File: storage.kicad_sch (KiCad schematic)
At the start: 0 parts

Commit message: Commit
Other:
- note added: "Simpler Flight v2"
- title: (none) -> Storage

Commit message: addecd stuff
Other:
- note added: "Flash Memory"
- note added: "SD Card"
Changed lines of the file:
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@@
 		(title "Storage")
 	)
+	(text "Flash Memory"
+		(exclude_from_sim no)
+		(at 38.608 23.114 0)
+		(effects
+			(font
+				(size 2.54 2.54)
+				(thickness 0.508)
+				(bold yes)
+			)
+		)
+	)
+	(text "SD Card"
+		(exclude_from_sim no)
+		(at 84.074 23.114 0)
+		(effects
+			(font
+				(size 2.54 2.54)
+				(thickness 0.508)
+				(bold yes)
+			)
+		)
+	)
 	(text "Simpler Flight v2\n"
 		(exclude_from_sim no)
@@
 		)
 	)
+	(polyline
+		(pts
+			(xy 76.2 25.4) (xy 119.38 25.4)
+		)
+		(stroke
+			(width 0)
+			(type default)
+		)
+	)
+	(polyline
+		(pts
+			(xy 25.4 25.4) (xy 68.58 25.4)
+		)
+		(stroke
+			(width 0)
+			(type default)
+		)
+	)
+	(polyline
+		(pts
+			(xy 25.4 58.42) (xy 25.4 25.4)
+		)
+		(stroke
+			(width 0)
+			(type default)
+		)
+	)
+	(polyline
+		(pts
+			(xy 119.38 25.4) (xy 119.38 58.42)
+		)
+		(stroke
+			(width 0)
+			(type default)
+		)
+	)
+	(polyline
+		(pts
+			(xy 68.58 58.42) (xy 25.4 58.42)
+		)
+		(stroke
+			(width 0)
+			(type default)
+		)
+	)
+	(polyline
+		(pts
+			(xy 76.2 58.42) (xy 76.2 25.4)
+		)
+		(stroke
+			(width 0)
+			(type default)
+		)
+	)
+	(polyline
+		(pts
+			(xy 68.58 25.4) (xy 68.58 58.42)
+		)
+		(stroke
+			(width 0)
+			(type default)
+		)
+	)
+	(polyline
+		(pts
+			(xy 119.38 58.42) (xy 76.2 58.42)
+		)
+		(stroke
+			(width 0)
+			(type default)
+		)
+	)
 	(image
 		(at 254.508 174.244)
@@
 			"AAAAAAAAAAAAAAAAAAAAAAAAAAAAAAAAAAAAAAAAAAAAAAAAAAAAAAAAAAAAAAAAAAAAAAAAAAAA"
 			"AAAAAAAAAAAAAAAAAAAAAAAAAAAAAAAAAAAAAAAAAAAAAAAAAAAAAAAAAAAAAAAAAAAAAAAAAAAA"
+			"AAAAAAAAAAAAAAAAAAAAAAAAAAAAAAAAAAAAAAAAAAAAAAAAAAAAAAAAAAAAAAAAAAAAAAAAAAAA"
+			"AAAAAAAAAAAAAAAAAAAAAAAAAAAAAAAAAAAAAAAAAAAAAAAAAAAAAAAAAAAAAAAAAAAAAAAAAAAA"
+			"AAAAAAAAAAAAAAAAAAAAAAAAAAAAAAAAAAAAAAAAAAAAAAAAAAAAAAAAAAAAAAAAAAAAAAAAAAAA"
+			"AAAAAAAAAAAAAAAAAAAAAAAAAAAAAAAAAAAAAAAAAAAAAAAAAAAAAAAAAAAAAAAAAAAAAAAAAAAA"
+			"AAAAAAAAAAAAAAAAAAAAAAAAAAAAAAAAAAAAAAAAAAAAAAAAAAAAAAAAAAAAAAAAAAAAAAAAAAAA"
+			"AAAAAAAAAAAAAAAAAAAAAAAAAAAAAAAAAAAAAAAAAAAAAAAAAAAAAAAAAAAAAAAAAAAAAAAAAAAA"
+			"AAAAAAAAAAAAAAAAAAAAAAAAAAAAAAAAAAAAAAAAAAAAAAAAAAAAAAAAAAAAAAAAAAAAAAAAAAAA"
+			"AAAAAAAAAAAAAAAAAAAAAAAAAAAAAAAAAAAAAAAAAAAAAAAAAAAAAAAAAAAAAAAAAAAAAAAAAAAA"
+			"AAAAAAAAAAAAAAAAAAAAAAAAAAAAAAAAAAAAAAAAAAAAAAAAAAAAAAAAAAAAAAAAAAAAAAAAAAAA"
+			"AAAAAAAAAAAAAAAAAAAAAAAAAAAAAAAAAAAAAAAAAAAAAAAAAAAAAAAAAAAAAAAAAAAAAAAAAAAA"
+			"AAAAAAAAAAAAAAAAAAAAAAAAAAAAAAAAAAAAAAAAAAAAAAAAAAAAAAAAAAAAAAAAAAAAAAAAAAAA"
+			"AAAAAAAAAAAAAAAAAAAAAAAAAAAAAAAAAAAAAAAAAAAAAAAAAAAAAAAAAAAAAAAAAAAAAAAAAAAA"
+			"AAAAAAAAAAAAAAAAAAAAAAAAAAAAAAAAAAAAAAAAAAAAAAAAAAAAAAAAAAAAAAAAAAAAAAAAAAAA"
+			"AAAAAAAAAAAAAAAAAAAAAAAAAAAAAAAAAAAAAAAAAAAAAAAAAAAAAAAAAAAAAAAAAAAAAAAAAAAA"
+			"AAAAAAAAAAAAAAAAAAAAAAAAAAAAAAAAAAAAAAAAAAAAAAAAAAAAAAAAAAAAAAAAAAAAAAAAAAAA"
+			"AAAAAAAAAAAAAAAAAAAAAAAAAAAAAAAAAAAAAAAAAAAAAAAAAAAAAAAAAAAAAAAAAAAAAAAAAAAA"
+			"AAAAAAAAAAAAAAAAAAAAAAAAAAAAAAAAAAAAAAAAAAAAAAAAAAAAAAAAAAAAAAAAAAAAAAAAAAAA"
+			"AAAAAAAAAAAAAAAAAAAAAAAAAAAAAAAAAAAAAAAAAAAAAAAAAAAAAAAAAAAAAAAAAAAAAAAAAAAA"

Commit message: Initiliase main components
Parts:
- added J14: DM3CS-SF, DM3CS_SF:HRS_DM3CS-SF, symbol DM3CS-SF:DM3CS-SF
- added U7: W25X40CLSNIG, W25X40CLSNIG:WIN_SN-8_WIN, symbol W25X40CLSNIG:W25X40CLSNIG

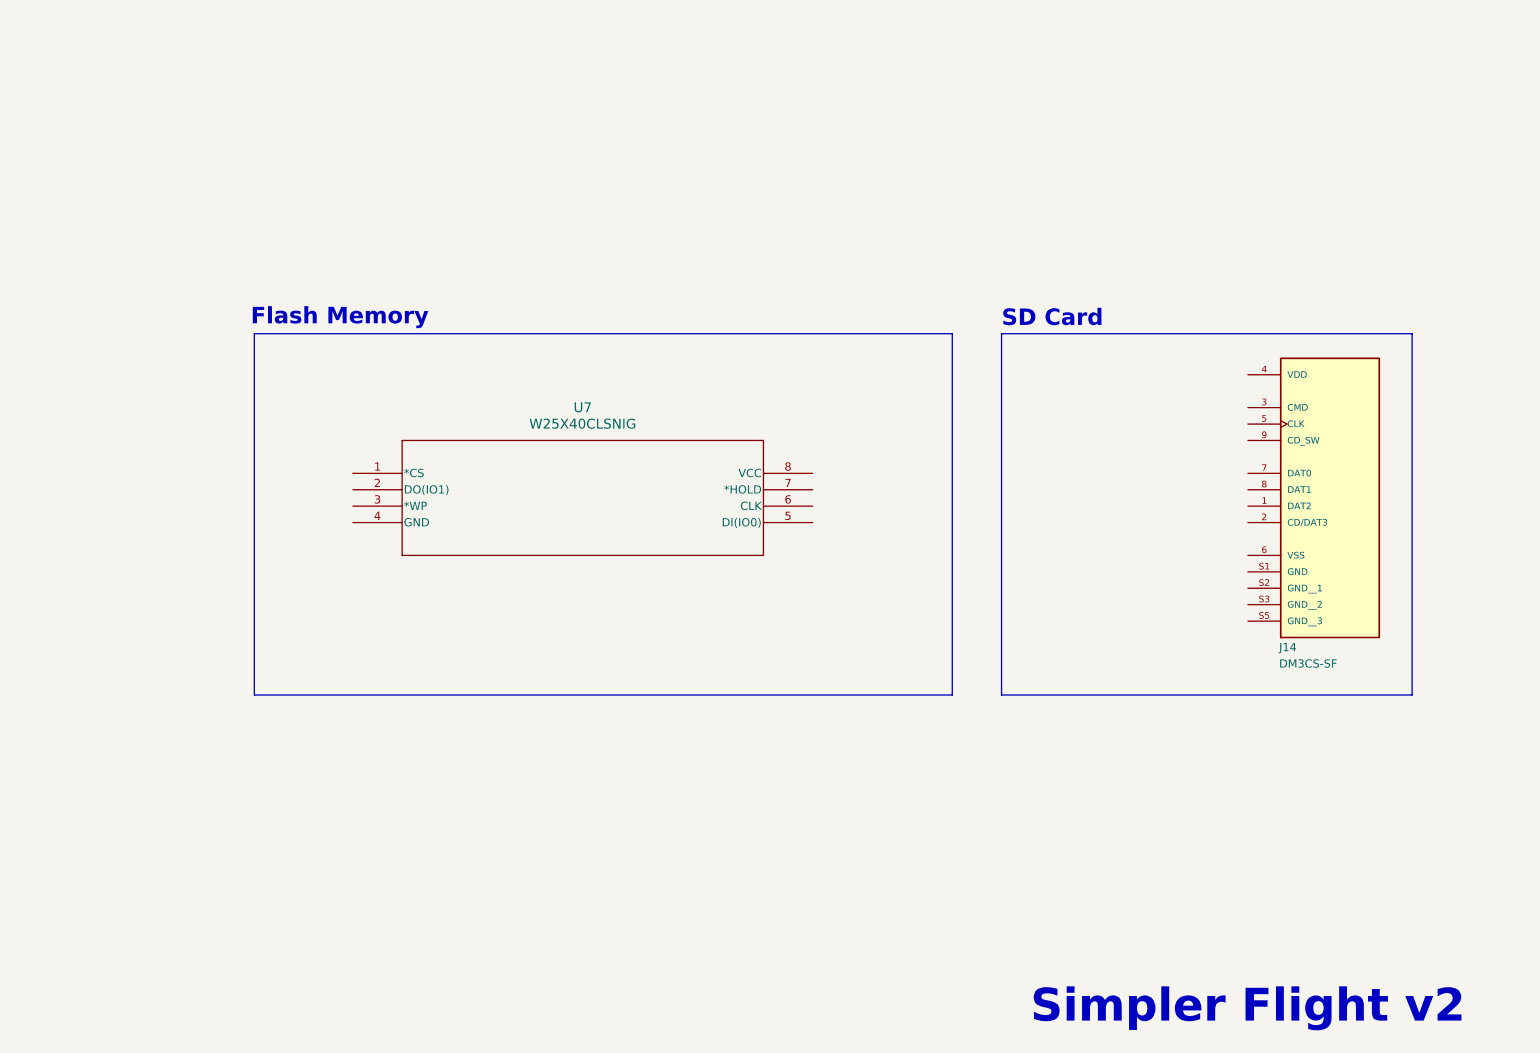
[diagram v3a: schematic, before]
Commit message: Update schematic, pending power sims, updated README
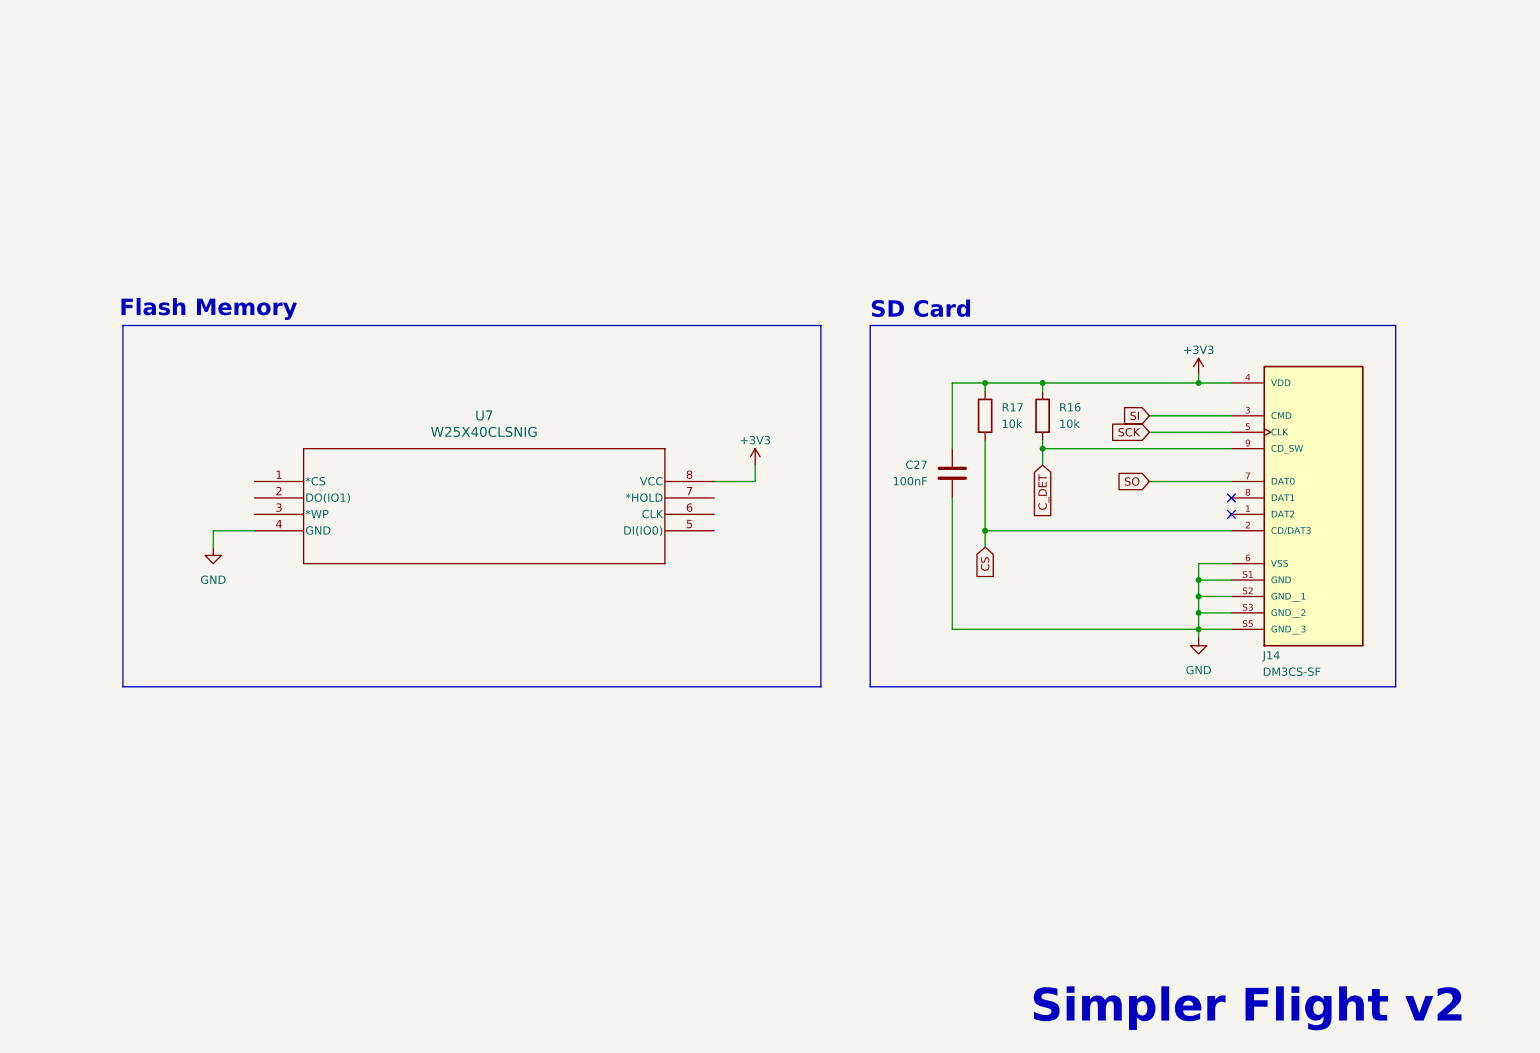
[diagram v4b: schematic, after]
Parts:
- added C27: 100nF, Capacitor_SMD:C_0805_2012Metric_Pad1.18x1.45mm_HandSolder, symbol Device:C
- added R16, R17: 10k, Resistor_SMD:R_0805_2012Metric_Pad1.20x1.40mm_HandSolder, symbol Device:R
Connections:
- net CS: now reaches J14.2 (CD/DAT3)
- net CS: now also R17.2
- net SI: now reaches J14.3 (CMD)
- net +3V3: now reaches J14.4 (VDD)
- net +3V3: now also U7.8 (VCC), C27.1, R16.1, R17.1
- net SCK: now reaches J14.5 (CLK)
- net GND: now reaches J14.6 (VSS)
- net GND: now also J14.S1 (GND), J14.S2 (GND__1), J14.S3 (GND__2), J14.S5 (GND__3), U7.4 (GND), C27.2
- net SO: now reaches J14.7 (DAT0)
- net C_DET: now reaches J14.9 (CD_SW)
- net C_DET: now also R16.2
- no-connect marks 0 -> 2
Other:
- moved on the sheet: J14, U7

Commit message: Updated schematics
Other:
- note added: "CAS Board 2025"
- note removed: "Simpler Flight v2"

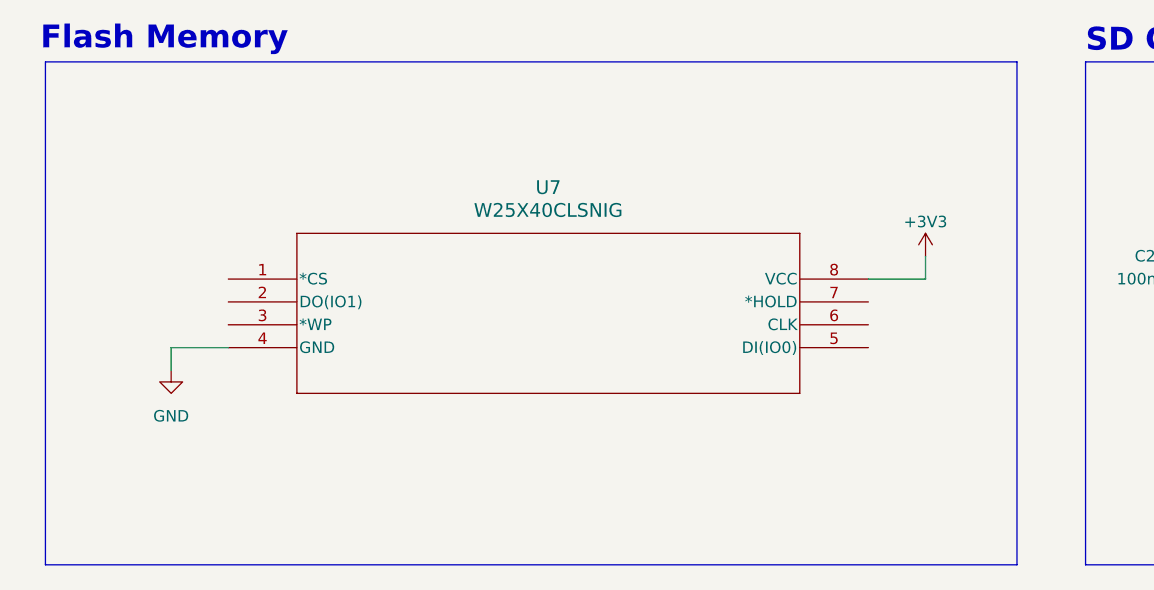
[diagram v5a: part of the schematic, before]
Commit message: Use different flash chip with nicer documentation
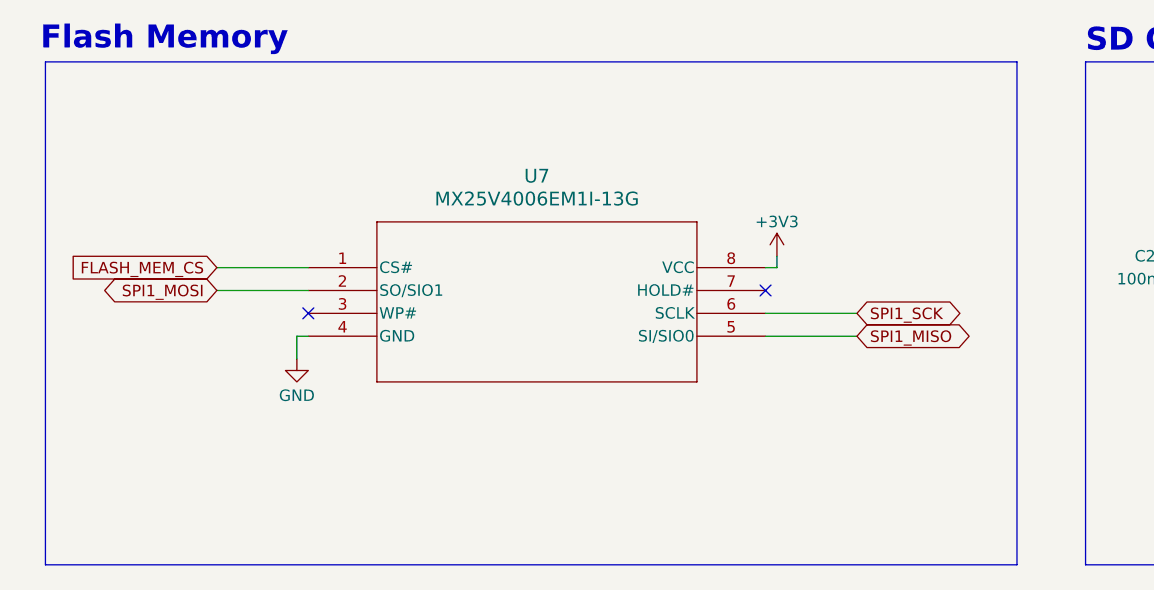
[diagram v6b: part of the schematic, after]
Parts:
- removed U7: W25X40CLSNIG, W25X40CLSNIG:WIN_SN-8_WIN, symbol W25X40CLSNIG:W25X40CLSNIG
- added U7: MX25V4006EM1I-13G, SOP8_150_MAC, symbol MX25V4006EM1I-13G:MX25V4006EM1I-13G
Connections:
- net +3V3: now also U7.8 (VCC)
- net GND: now also U7.4 (GND)
- new net FLASH_MEM_CS: U7.1 (CS#)
- new net SPI1_MISO: U7.5 (SI/SIO0)
- new net SPI1_MOSI: U7.2 (SO/SIO1)
- new net SPI1_SCK: U7.6 (SCLK)
- no-connect marks 2 -> 4

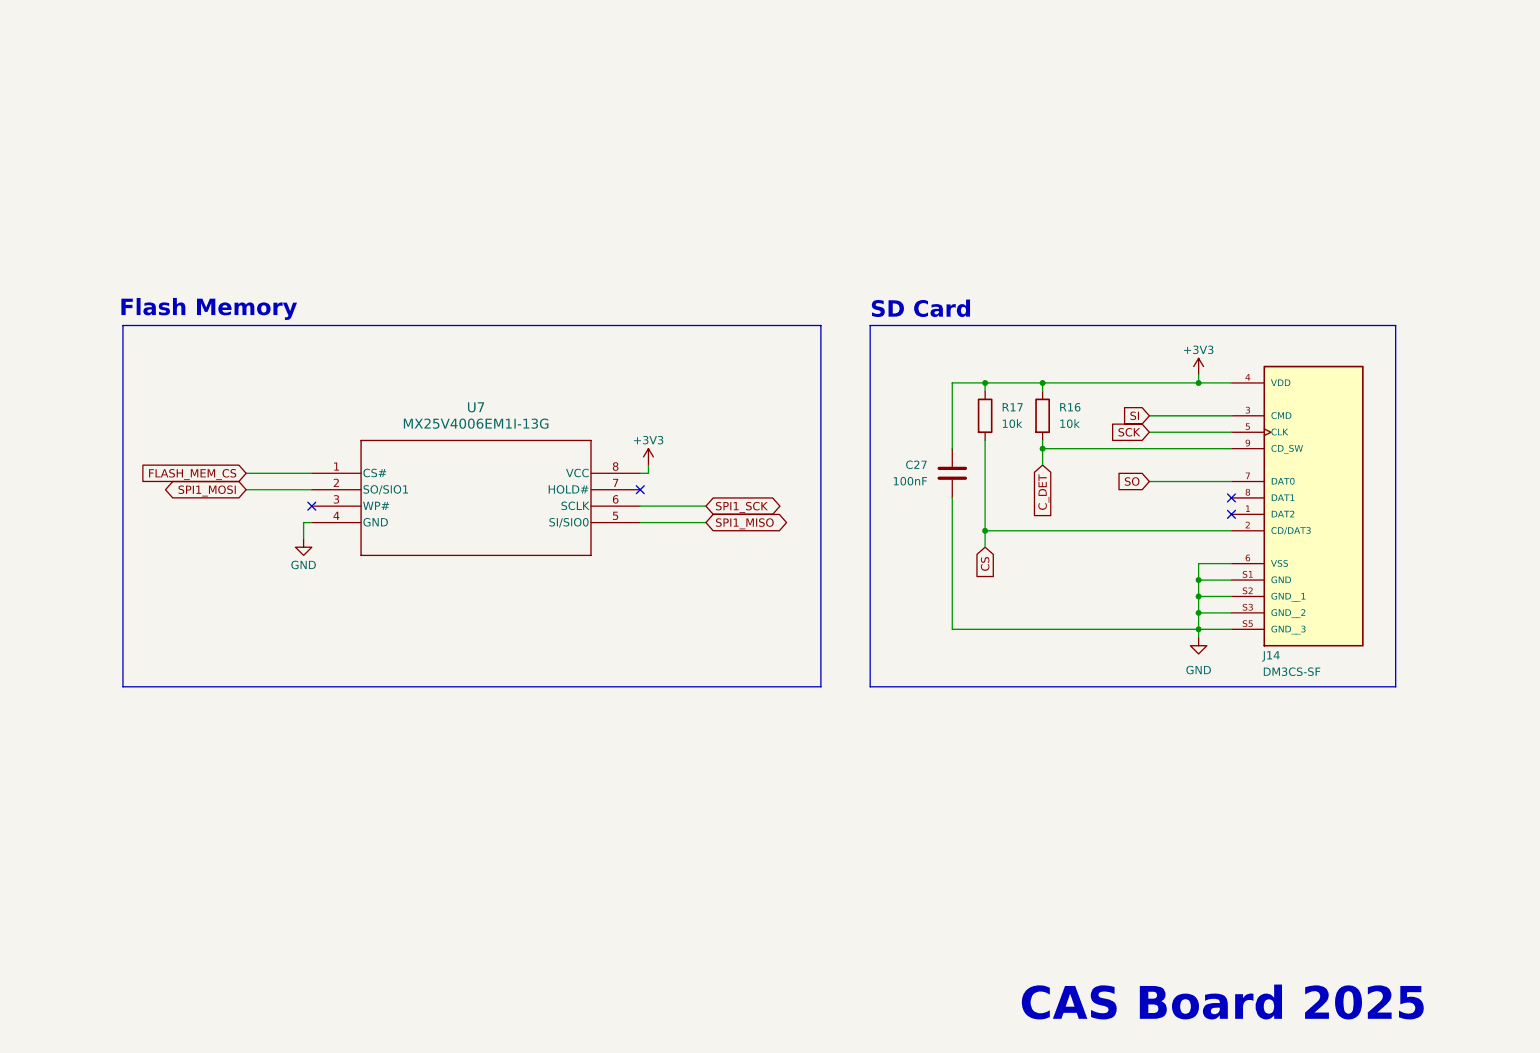
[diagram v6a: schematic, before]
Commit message: labels for storage schematic
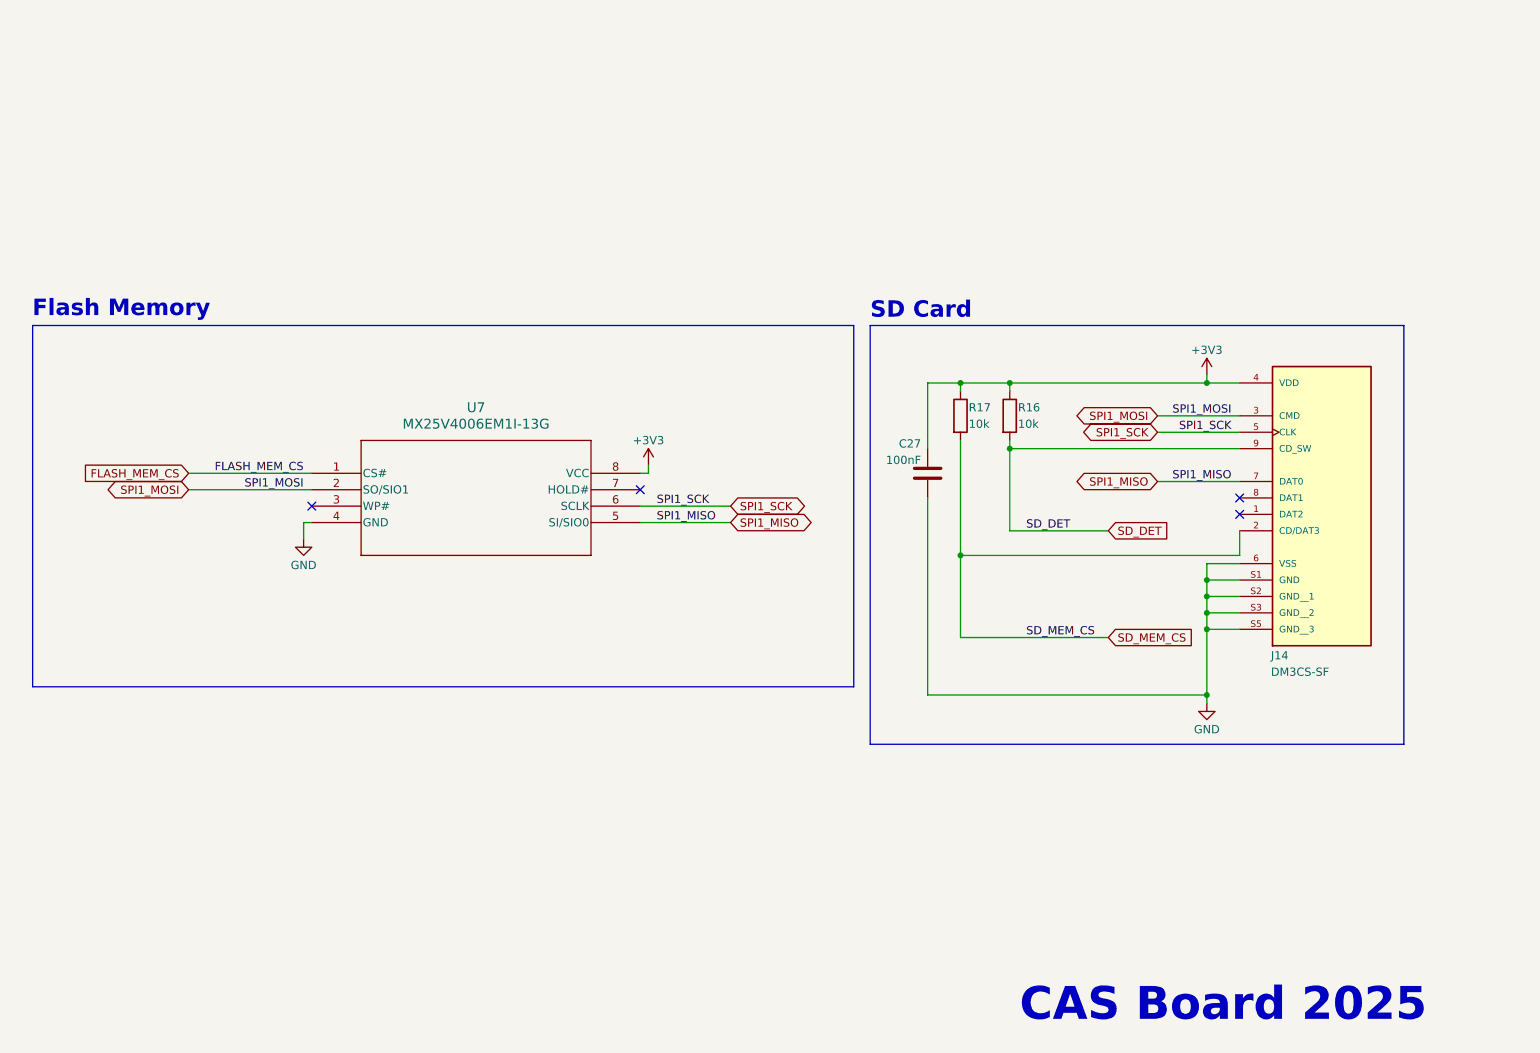
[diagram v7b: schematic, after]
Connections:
- net SCK is gone; now on net SPI1_SCK: J14.5 (CLK)
- net SI is gone; now on net SPI1_MOSI: J14.3 (CMD)
- net SO is gone; now on net SPI1_MISO: J14.7 (DAT0)
- net CS renamed SD_MEM_CS
- net C_DET renamed SD_DET
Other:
- moved on the sheet: C27, J14, R16, R17
